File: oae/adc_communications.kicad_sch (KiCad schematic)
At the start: 3 parts

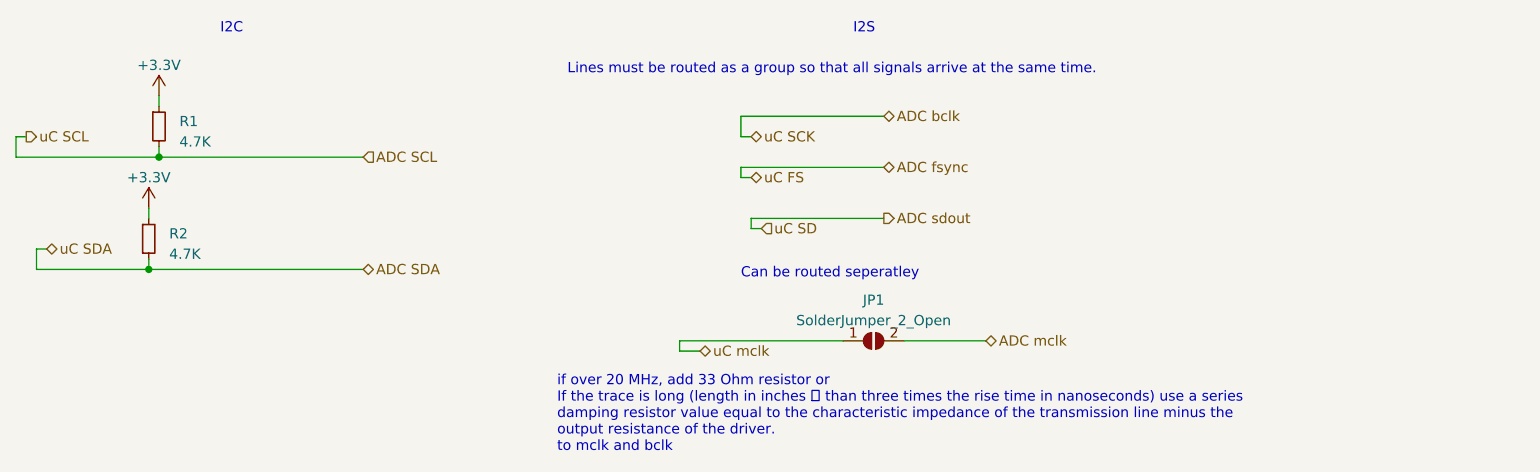
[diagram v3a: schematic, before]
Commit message: Routed ADC to MSC
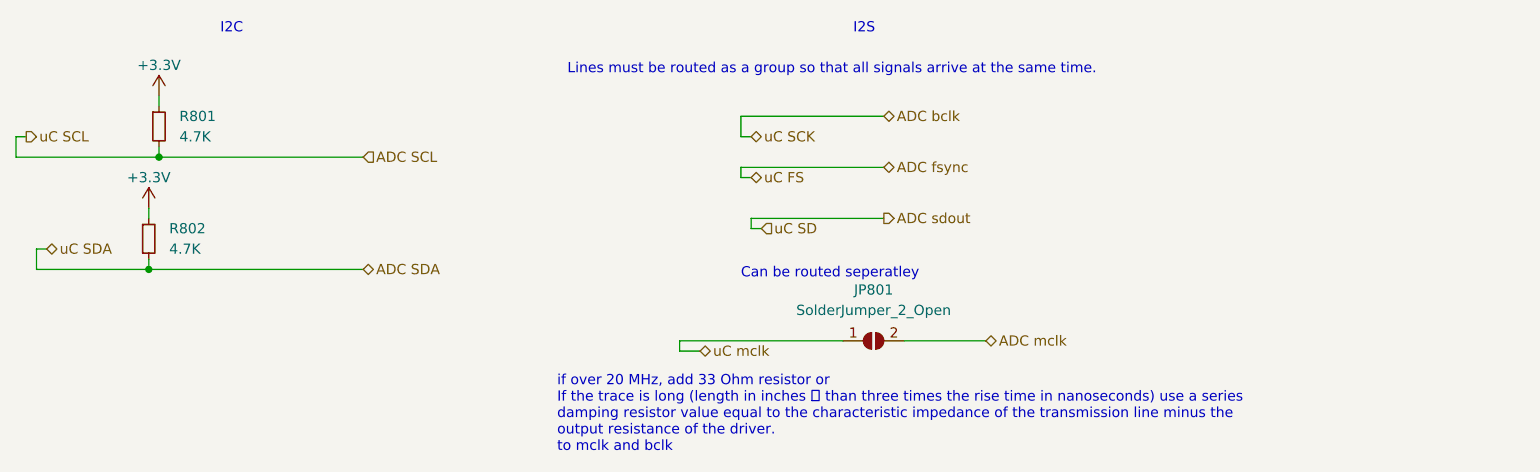
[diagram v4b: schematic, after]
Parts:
- R801: renamed from R1; footprint (none) -> Resistor_SMD:R_0603_1608Metric_Pad0.98x0.95mm_HandSolder
- renumbered JP1 to JP801, R2 to R802
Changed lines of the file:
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@@
   (symbol (lib_id "Jumper:SolderJumper_2_Open") (at 184.15 102.87 0) (unit 1)
     (in_bom yes) (on_board yes) (dnp no) (fields_autoplaced)
-    (property "Reference" "JP1" (at 184.15 97.79 0)
+    (property "Reference" "JP801" (at 184.15 96.52 0)
       (effects (font (size 1.27 1.27)))
     )
-    (property "Value" "SolderJumper_2_Open" (at 184.15 100.33 0)
+    (property "Value" "SolderJumper_2_Open" (at 184.15 99.06 0)
       (effects (font (size 1.27 1.27)))
     )
@@
       (project "oae"
         (path "/e63e39d7-6ac0-4ffd-8aa3-1841a4541b55/f5ec4301-2f32-46c4-8f0d-2c5a15cb6fc4/2604763a-d7f3-46e8-b8fe-c57329b542da"
-          (reference "JP1") (unit 1)
+          (reference "JP801") (unit 1)
         )
       )
@@
   (symbol (lib_id "Device:R_Small") (at 95.25 76.2 0) (unit 1)
     (in_bom yes) (on_board yes) (dnp no) (fields_autoplaced)
-    (property "Reference" "R1" (at 97.79 75.565 0)
+    (property "Reference" "R801" (at 97.79 74.93 0)
       (effects (font (size 1.27 1.27)) (justify left))
     )
-    (property "Value" "4.7K" (at 97.79 78.105 0)
+    (property "Value" "4.7K" (at 97.79 77.47 0)
       (effects (font (size 1.27 1.27)) (justify left))
     )
-    (property "Footprint" "" (at 95.25 76.2 0)
+    (property "Footprint" "Resistor_SMD:R_0603_1608Metric_Pad0.98x0.95mm_HandSolder" (at 95.25 76.2 0)
       (effects (font (size 1.27 1.27)) hide)
     )
@@
       (project "oae"
         (path "/e63e39d7-6ac0-4ffd-8aa3-1841a4541b55/f5ec4301-2f32-46c4-8f0d-2c5a15cb6fc4/2604763a-d7f3-46e8-b8fe-c57329b542da"
-          (reference "R1") (unit 1)
+          (reference "R801") (unit 1)
         )
       )
@@
   (symbol (lib_id "power:+3.3V") (at 93.98 86.36 0) (unit 1)
     (in_bom yes) (on_board yes) (dnp no) (fields_autoplaced)
-    (property "Reference" "#PWR02" (at 93.98 90.17 0)
+    (property "Reference" "#PWR0105" (at 93.98 90.17 0)
       (effects (font (size 1.27 1.27)) hide)
     )
@@
       (project "oae"
         (path "/e63e39d7-6ac0-4ffd-8aa3-1841a4541b55/f5ec4301-2f32-46c4-8f0d-2c5a15cb6fc4/2604763a-d7f3-46e8-b8fe-c57329b542da"
-          (reference "#PWR02") (unit 1)
+          (reference "#PWR0105") (unit 1)
         )
       )
@@
   (symbol (lib_id "power:+3.3V") (at 95.25 72.39 0) (unit 1)
     (in_bom yes) (on_board yes) (dnp no) (fields_autoplaced)
-    (property "Reference" "#PWR01" (at 95.25 76.2 0)
+    (property "Reference" "#PWR0106" (at 95.25 76.2 0)
       (effects (font (size 1.27 1.27)) hide)
     )
@@
       (project "oae"
         (path "/e63e39d7-6ac0-4ffd-8aa3-1841a4541b55/f5ec4301-2f32-46c4-8f0d-2c5a15cb6fc4/2604763a-d7f3-46e8-b8fe-c57329b542da"
-          (reference "#PWR01") (unit 1)
+          (reference "#PWR0106") (unit 1)
         )
       )
@@
   (symbol (lib_id "Device:R_Small") (at 93.98 90.17 0) (unit 1)
     (in_bom yes) (on_board yes) (dnp no) (fields_autoplaced)
-    (property "Reference" "R2" (at 96.52 89.535 0)
+    (property "Reference" "R802" (at 96.52 88.9 0)
       (effects (font (size 1.27 1.27)) (justify left))
     )
-    (property "Value" "4.7K" (at 96.52 92.075 0)
+    (property "Value" "4.7K" (at 96.52 91.44 0)
       (effects (font (size 1.27 1.27)) (justify left))
     )
@@
       (project "oae"
         (path "/e63e39d7-6ac0-4ffd-8aa3-1841a4541b55/f5ec4301-2f32-46c4-8f0d-2c5a15cb6fc4/2604763a-d7f3-46e8-b8fe-c57329b542da"
-          (reference "R2") (unit 1)
+          (reference "R802") (unit 1)
         )
       )
